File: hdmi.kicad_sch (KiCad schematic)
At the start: 11 parts, among them J2101 FPC0.5-SMT-20P, U2101 RCLAMP0524P, U2102 RCLAMP0524P, U2103 RCLAMP0524P, U2104 AP22653W6-7

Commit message: Add comments about diff pair polarity
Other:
- note added: "HDMI diff pair polarity MUST be maintained."
- note removed: "Note that the FFC connector pin numbering is reversed relative to HDMI pinout."
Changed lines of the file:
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@@
 		(comment 3 "HALPI2 is licensed under CERN-OHL-S v2.")
 	)
-	(text "Note that the FFC connector pin \nnumbering is reversed relative to HDMI\npinout."
+	(text "HDMI diff pair polarity\nMUST be maintained."
 		(exclude_from_sim no)
 		(at 250.19 58.42 0)

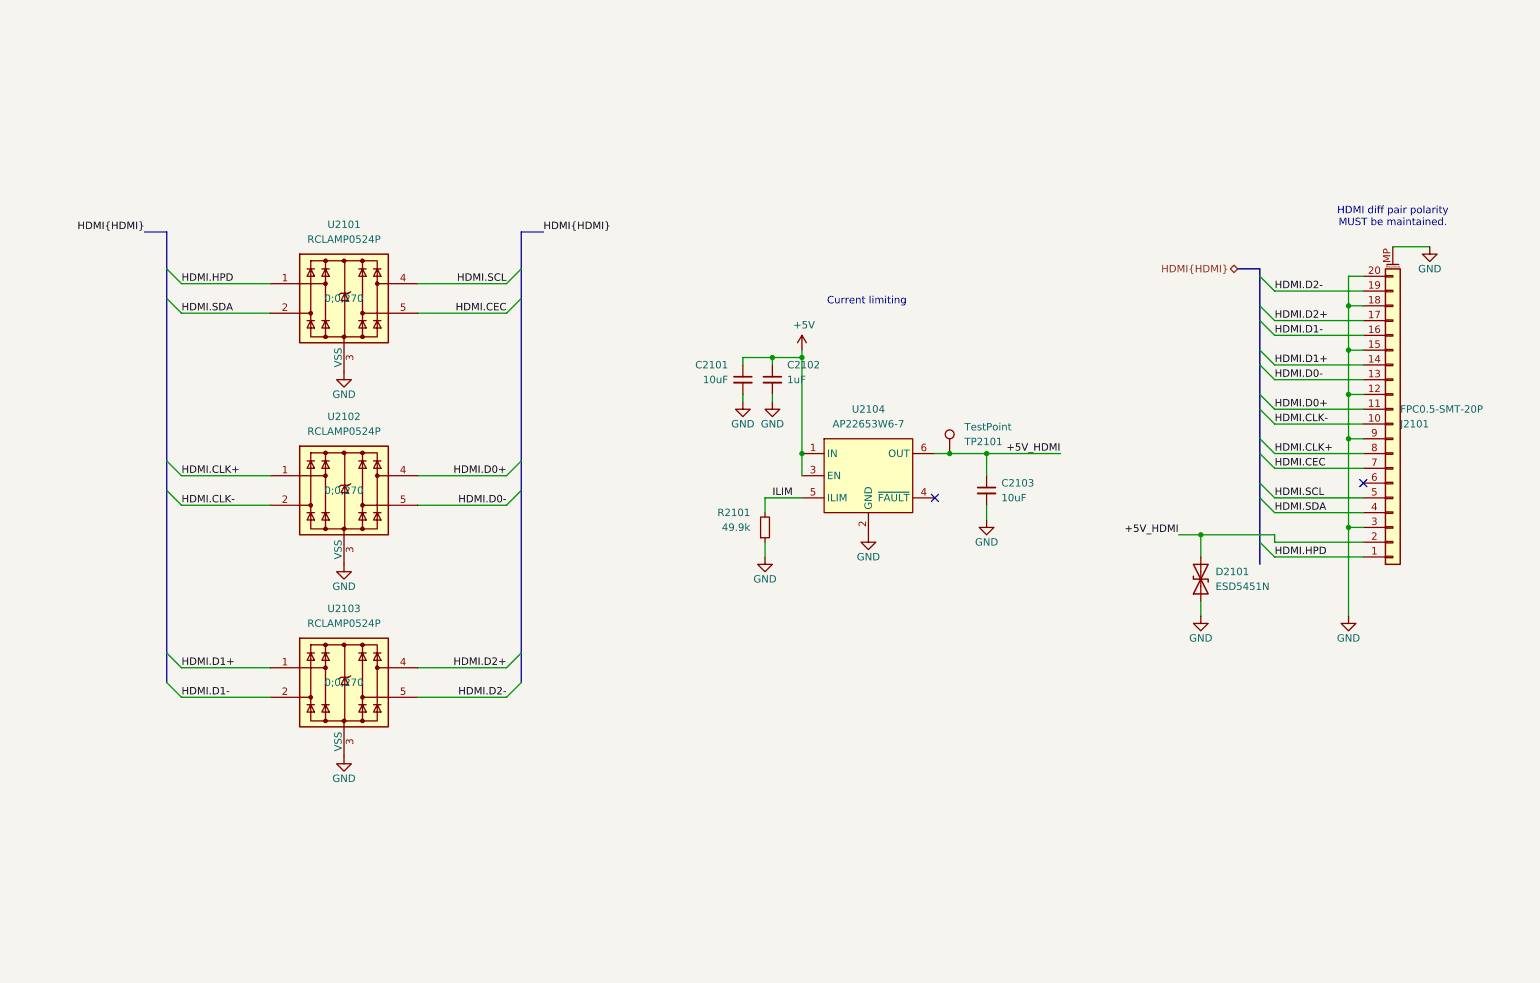
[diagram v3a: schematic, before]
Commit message: Fix HDMI pinout
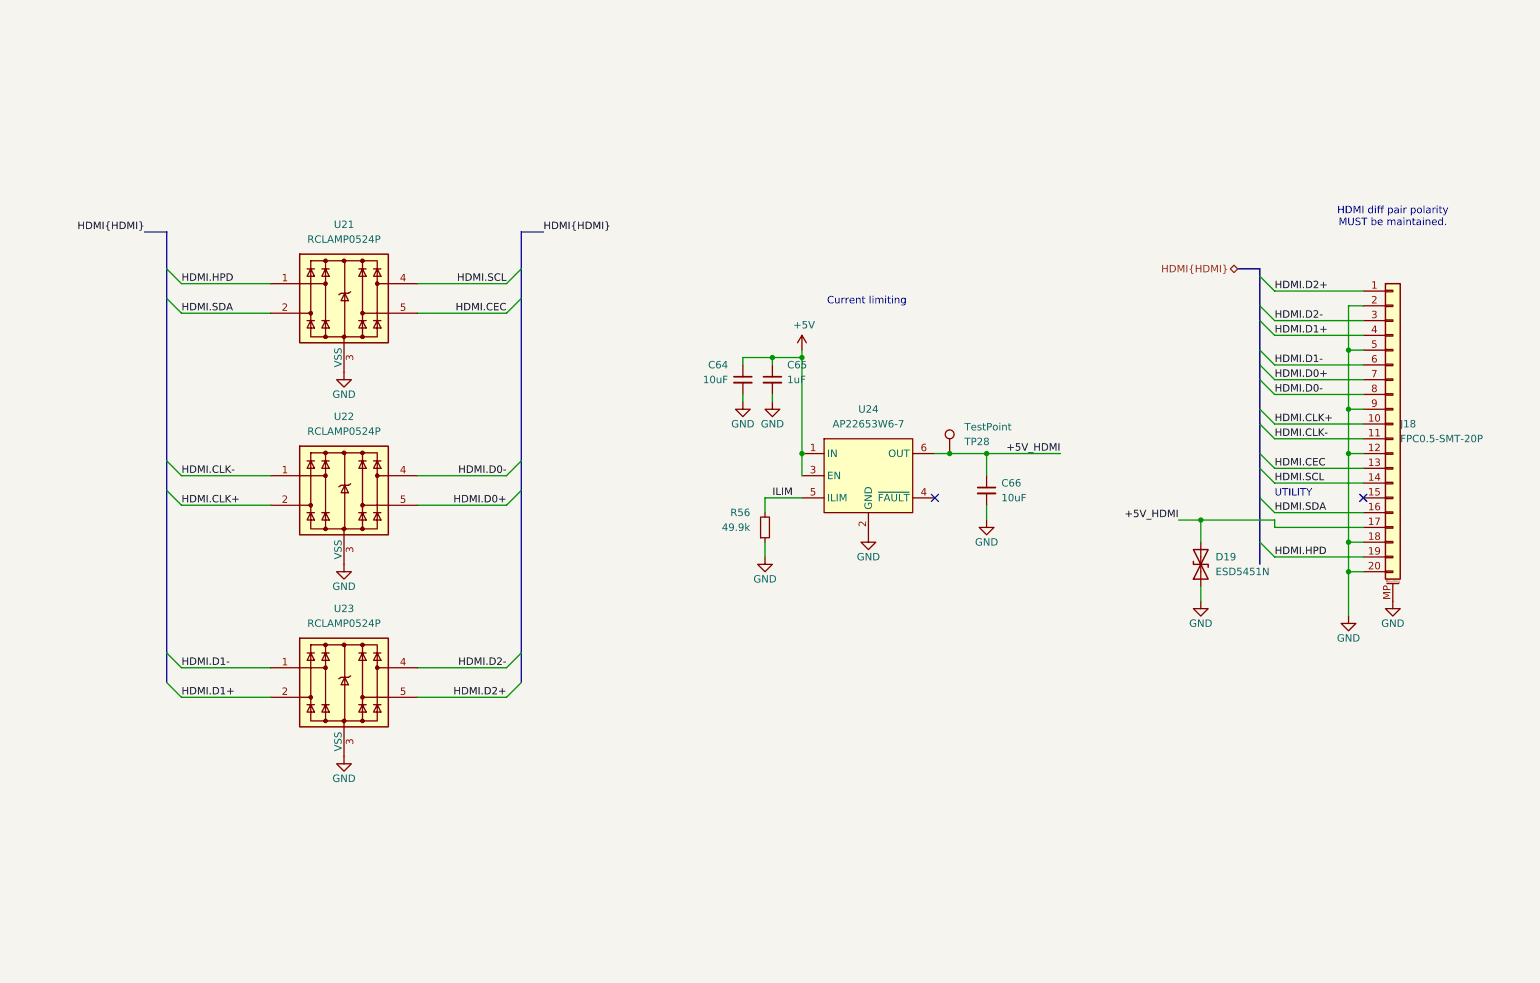
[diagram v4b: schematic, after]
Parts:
- J18: renamed from J2101; footprint Hatlabs:FFC_HDGC_0.5K-A-20PB_1x20-1SV_P0.5mm_Vertical -> HL_Connector:FFC_1x20_JUSHUO_AFC11-S20ICC-00_P0.5mm_Vertical
- renumbered C2101 to C64, C2102 to C65, C2103 to C66, D2101 to D19, R2101 to R56, TP2101 to TP28, U2101 to U21, U2102 to U22, U2103 to U23, U2104 to U24
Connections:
- net +5V_HDMI: now also J18.17 (Pin_17); no longer J18.2 (Pin_2)
- net GND: now also J18.2 (Pin_2), J18.5 (Pin_5); no longer J18.15 (Pin_15), J18.3 (Pin_3)
- net HDMI.CEC: now also J18.13 (Pin_13); no longer J18.7 (Pin_7)
- net HDMI.CLK+: now also J18.10 (Pin_10), U22.2, U22.9; no longer J18.8 (Pin_8), U22.1, U22.10
- net HDMI.CLK-: now also J18.11 (Pin_11), U22.1, U22.10; no longer J18.10 (Pin_10), U22.2, U22.9
- net HDMI.D0+: now also J18.7 (Pin_7), U22.5, U22.6; no longer J18.11 (Pin_11), U22.4, U22.7
- net HDMI.D0-: now also J18.8 (Pin_8), U22.4, U22.7; no longer J18.13 (Pin_13), U22.5, U22.6
- net HDMI.D1+: now also J18.4 (Pin_4), U23.2, U23.9; no longer J18.14 (Pin_14), U23.1, U23.10
- net HDMI.D1-: now also J18.6 (Pin_6), U23.1, U23.10; no longer J18.16 (Pin_16), U23.2, U23.9
- net HDMI.D2+: now also J18.1 (Pin_1), U23.5, U23.6; no longer J18.17 (Pin_17), U23.4, U23.7
- net HDMI.D2-: now also J18.3 (Pin_3), U23.4, U23.7; no longer J18.19 (Pin_19), U23.5, U23.6
- net HDMI.HPD: now also J18.19 (Pin_19); no longer J18.1 (Pin_1)
- net HDMI.SCL: now also J18.14 (Pin_14); no longer J18.5 (Pin_5)
- net HDMI.SDA: now also J18.16 (Pin_16); no longer J18.4 (Pin_4)
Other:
- note added: "UTILITY"
- moved on the sheet: D19, J18

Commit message: Reannotate the board
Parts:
- renumbered C64 to C65, C65 to C66, C66 to C67, D19 to D18, J18 to J17, TP28 to TP27, U21 to U20, U22 to U21, U23 to U22, U24 to U23

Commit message: FInal v0.2.0 proto changes
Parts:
- renumbered C65 to C67, C66 to C68, C67 to C69, TP27 to TP36, U23 to U20, U20 to U21, U21 to U22, U22 to U23
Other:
- note added: "AUX GND"
- note added: "CLK GND"
- note added: "D0 GND"
- note added: "D1 GND"
- note added: "D2 GND"
- note added: "P1"
- note added: "P10"
- note added: "P11"
- note added: "P12"
- note added: "P13"
- note added: "P14"
- note added: "P15"
- note added: "P16"
- note added: "P17"
- note added: "P18"
- note added: "P19"
- note added: "P2"
- note added: "P3"
- note added: "P4"
- note added: "P5"
- note added: "P6"
- note added: "P7"
- note added: "P8"
- note added: "P9"
- moved on the sheet: C67, C68, C69, D18, J17, R56, TP36, U20, U21, U22, U23
